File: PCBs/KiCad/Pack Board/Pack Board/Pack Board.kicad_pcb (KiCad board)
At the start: 2 copper layers, 10 parts, among them J4 BAR, J5 DISP, U1 Teensy4.0_AudioShield_REVD, U2 74AHC125

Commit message: Wand Board Updates
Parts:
- added J1: VENT LIGHTS, Connector_JST:JST_XH_B3B-XH-A_1x03_P2.50mm_Vertical, F.Cu at (251.2, 127.7)
- added J10: SND OUT, Connector_JST:JST_XH_B2B-XH-A_1x02_P2.50mm_Vertical, F.Cu at (181.9, 93.6)
- added J11: SND IN R, Connector_JST:JST_XH_B2B-XH-A_1x02_P2.50mm_Vertical, F.Cu at (205.7, 133.0)
- added J12: SND IN L, Connector_JST:JST_XH_B2B-XH-A_1x02_P2.50mm_Vertical, F.Cu at (205.7, 140.8)
- added J13: BT MOSFET, Connector_JST:JST_XH_B3B-XH-A_1x03_P2.50mm_Vertical, F.Cu at (251.2, 151.1)
- added J14: VENT MOSFET, Connector_JST:JST_XH_B3B-XH-A_1x03_P2.50mm_Vertical, F.Cu at (251.2, 158.9)
- added J15: ROT ENC, Connector_JST:JST_XH_B3B-XH-A_1x03_P2.50mm_Vertical, F.Cu at (251.2, 166.7)
- added J16: ROT SW, Connector_JST:JST_XH_B2B-XH-A_1x02_P2.50mm_Vertical, F.Cu at (205.7, 148.6)
- added J17: ION SW, Connector_JST:JST_XH_B2B-XH-A_1x02_P2.50mm_Vertical, F.Cu at (126.5, 145.5)
- added J2: PCELL LIGHTS, Connector_JST:JST_XH_B3B-XH-A_1x03_P2.50mm_Vertical, F.Cu at (155.5, 145.5)
- added J3: CYCLO LIGHTS, Connector_JST:JST_XH_B3B-XH-A_1x03_P2.50mm_Vertical, F.Cu at (251.2, 143.3)
- added J6: SERIAL, TerminalBlock_Phoenix:TerminalBlock_Phoenix_MKDS-1,5-2_1x02_P5.00mm_Horizontal, F.Cu at (137.5, 87.0)
- added J7: POW_IN, TerminalBlock_Phoenix:TerminalBlock_Phoenix_MKDS-1,5-2_1x02_P5.00mm_Horizontal, F.Cu at (106.0, 110.0)
- added J8: WAND PWR, TerminalBlock_Phoenix:TerminalBlock_Phoenix_MKDS-1,5-2_1x02_P5.00mm_Horizontal, F.Cu at (149.0, 87.0)
- added J9: AMP VOL, Connector_JST:JST_XH_B4B-XH-A_1x04_P2.50mm_Vertical, F.Cu at (227.2, 125.2)
- added REF**: MountingHole_3.2mm_M3_DIN965_Pad, MountingHole:MountingHole_3.2mm_M3_DIN965_Pad, F.Cu at (105.0, 145.0)
- added REF**: MountingHole_3.2mm_M3_DIN965_Pad, MountingHole:MountingHole_3.2mm_M3_DIN965_Pad, F.Cu at (170.0, 85.0)
- added REF**: MountingHole_3.2mm_M3_DIN965_Pad, MountingHole:MountingHole_3.2mm_M3_DIN965_Pad, F.Cu at (170.0, 145.0)
- added REF**: MountingHole_3.2mm_M3_DIN965_Pad, MountingHole:MountingHole_3.2mm_M3_DIN965_Pad, F.Cu at (105.0, 85.0)
- moved R4 147.0 mm to (243.1, 33.9), turned to -90 degrees
- moved R5 144.9 mm to (239.0, 33.9), turned to -90 degrees
- moved J4 123.1 mm to (237.1, 62.1)
- moved J5 123.1 mm to (237.1, 69.9)
- moved R3 103.3 mm to (199.6, 39.5), turned to 180 degrees
- moved C1 97.4 mm to (183.5, 37.0)
- moved R2 89.2 mm to (192.3, 56.0), turned to 180 degrees
- moved U2 62.2 mm to (166.5, 37.5)
- moved U1 51.6 mm to (131.0, 106.0), turned to -90 degrees
- moved R1 39.3 mm to (138.0, 52.5)
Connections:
- C1 pad 1: Net-(J1-Pin_2) -> +5V
- C1 pad 2: Net-(J1-Pin_1) -> GND
- J4 pad 1: Net-(J4-Pin_1) -> GND
- J4 pad 2: Net-(J4-Pin_2) -> +3.3V
- J4 pad 4: /SCL -> Net-(J4-Pin_4)
- J5 pad 1: Net-(J4-Pin_1) -> GND
- J5 pad 2: Net-(J4-Pin_2) -> +3.3V
- J5 pad 4: /SCL -> Net-(J4-Pin_4)
- R4 pad 2: Net-(J4-Pin_2) -> +3.3V
- R5 pad 1: /SCL -> Net-(J4-Pin_4)
- R5 pad 2: Net-(J4-Pin_2) -> +3.3V
- U1 pad 1: unconnected-(U1-GND-Pad1) -> GND
- U1 pad 11: unconnected-(U1-9_OUT1C-Pad11) -> Net-(J16-Pin_2)
- U1 pad 18: unconnected-(U1-14_A0_TX3_SPDIF_OUT-Pad18) -> Net-(U1-14_A0_TX3_SPDIF_OUT)
- U1 pad 2: unconnected-(U1-0_RX1_CRX2_CS1-Pad2) -> /RX
- U1 pad 20: unconnected-(U1-16_A2_RX4_SCL1-Pad20) -> Net-(U1-16_A2_RX4_SCL1)
- U1 pad 21: unconnected-(U1-17_A3_TX4_SDA1-Pad21) -> Net-(U1-17_A3_TX4_SDA1)
- U1 pad 22: unconnected-(U1-18_A4_SDA0-Pad22) -> /SDA
- U1 pad 23: unconnected-(U1-19_A5_SCL0-Pad23) -> Net-(J4-Pin_4)
- U1 pad 26: unconnected-(U1-22_A8_CTX1-Pad26) -> Net-(J17-Pin_2)
- U1 pad 28: unconnected-(U1-3V-Pad28) -> +3.3V
- U1 pad 29: unconnected-(U1-GND-Pad29) -> GND
- U1 pad 3: unconnected-(U1-1_TX1_CTX2_MISO1-Pad3) -> /TX
- U1 pad 30: unconnected-(U1-5V-Pad30) -> +5V
- U1 pad 31: unconnected-(U1-LINE_OUT_L-Pad31) -> Net-(J10-Pin_2)
- U1 pad 32: unconnected-(U1-LINE_OUT_GND-Pad32) -> Net-(J10-Pin_1)
- U1 pad 34: unconnected-(U1-LINE_IN_R-Pad34) -> Net-(J11-Pin_2)
- U1 pad 35: unconnected-(U1-LINE_IN_L-Pad35) -> Net-(J12-Pin_2)
- U1 pad 36: unconnected-(U1-LINE_IN_R_GND-Pad36) -> Net-(J11-Pin_1)
- U1 pad 37: unconnected-(U1-LINE_IN_L_GND-Pad37) -> Net-(J12-Pin_1)
- U1 pad 4: unconnected-(U1-2_OUT2-Pad4) -> Net-(J15-Pin_1)
- U1 pad 5: unconnected-(U1-3_LRCLK2-Pad5) -> Net-(J13-Pin_3)
- U1 pad 6: unconnected-(U1-4_BCLK2-Pad6) -> Net-(J15-Pin_3)
- U1 pad 7: unconnected-(U1-5_IN2-Pad7) -> Net-(J14-Pin_3)
- U2 pad 10: unconnected-(U2-3OE-Pad10) -> GND
- U2 pad 12: unconnected-(U2-4A-Pad12) -> Net-(U1-14_A0_TX3_SPDIF_OUT)
- U2 pad 13: Net-(U2-2OE) -> GND
- U2 pad 14: unconnected-(U2-VCC-Pad14) -> +5V
- U2 pad 4: Net-(U2-2OE) -> GND
- U2 pad 5: unconnected-(U2-2A-Pad5) -> Net-(U1-17_A3_TX4_SDA1)
- U2 pad 7: Net-(U2-2OE) -> GND
- U2 pad 9: unconnected-(U2-3A-Pad9) -> Net-(U1-16_A2_RX4_SCL1)
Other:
- board outline added: 75 x 70 mm

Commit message: Added motor output for wand rumble
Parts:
- added J18: i2c Extend, Connector_JST:JST_XH_B4B-XH-A_1x04_P2.50mm_Vertical, F.Cu at (227.2, 117.0)

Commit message: Added additional i2c output to wand board for optional driver
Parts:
- removed J4: BAR, Connector_JST:JST_XH_B4B-XH-A_1x04_P2.50mm_Vertical
- removed J5: DISP, Connector_JST:JST_XH_B4B-XH-A_1x04_P2.50mm_Vertical
- moved J18 30.1 mm to (237.5, 88.8)
- moved J9 25.8 mm to (237.5, 101.5)
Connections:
- net Net-(J18-Pin_4) renamed /SCL
- U1 pad 45: (no net) -> unconnected-(U1-NCB-Pad45)
- U1 pad 46: (no net) -> unconnected-(U1-NCA-Pad46)

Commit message: Pack Board 2.0
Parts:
- moved J15 160.3 mm to (104.2, 102.8)
- moved J13 152.0 mm to (104.2, 112.5)
- moved J3 139.9 mm to (120.2, 94.2)
- moved J1 137.9 mm to (120.2, 84.5)
- moved C1 125.6 mm to (106.0, 135.8)
- moved J14 120.5 mm to (156.5, 84.5)
- moved R3 120.1 mm to (118.2, 127.9), turned to 90 degrees
- moved J16 114.5 mm to (105.5, 93.2)
- moved R4 111.9 mm to (151.1, 97.8), turned to 180 degrees
- moved R5 111.0 mm to (151.1, 101.8), turned to 180 degrees
- moved R2 100.9 mm to (121.5, 127.9), turned to 90 degrees
- moved U2 82.3 mm to (114.8, 101.5)
- moved J9 80.4 mm to (157.5, 93.5), turned to -90 degrees
- moved R1 78.8 mm to (115.0, 127.9), turned to 90 degrees
- moved J18 70.7 mm to (167.0, 93.5), turned to -90 degrees
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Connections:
- net /SCL renamed Net-(J18-Pin_4)
- net Net-(J10-Pin_1) renamed /LINE_OUT_GND
- net Net-(J11-Pin_1) renamed /LINE_IN_R_GND
- net Net-(J11-Pin_2) renamed /LINE_IN_R
- net Net-(J12-Pin_1) renamed /LINE_IN_L_GND
- net Net-(J12-Pin_2) renamed /LINE_IN_L
- J10 pad 2: Net-(J10-Pin_2) -> /LINE_OUT_L
- U1 pad 11: Net-(J16-Pin_2) -> Net-(J13-Pin_3)
- U1 pad 31: Net-(J10-Pin_2) -> /LINE_OUT_L
- U1 pad 4: Net-(J15-Pin_1) -> Net-(J16-Pin_2)
- U1 pad 46: unconnected-(U1-NCA-Pad46) -> /LINE_OUT_L
- U1 pad 5: Net-(J13-Pin_3) -> Net-(J15-Pin_3)
- U1 pad 6: Net-(J15-Pin_3) -> Net-(J15-Pin_1)
- U2 pad 12: Net-(U1-14_A0_TX3_SPDIF_OUT) -> Net-(U1-17_A3_TX4_SDA1)
- U2 pad 5: Net-(U1-17_A3_TX4_SDA1) -> Net-(U1-14_A0_TX3_SPDIF_OUT)
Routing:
- net +3.3V: track 0.00 -> 167.0 mm
- net +5V: track 0.00 -> 156.9 mm
- net Net-(J16-Pin_2): track 0.00 -> 63.1 mm
- net Net-(J17-Pin_2): track 0.00 -> 63.1 mm
- net Net-(U1-14_A0_TX3_SPDIF_OUT): track 0.00 -> 61.9 mm
- net Net-(J15-Pin_1): track 0.00 -> 55.6 mm
- net Net-(J15-Pin_3): track 0.00 -> 53.4 mm
- net Net-(J14-Pin_3): track 0.00 -> 51.2 mm
- net Net-(J1-Pin_3): track 0.00 -> 48.4 mm
- net /SDA: track 0.00 -> 47.3 mm
- net Net-(J13-Pin_3): track 0.00 -> 43.6 mm
- net Net-(U1-17_A3_TX4_SDA1): track 0.00 -> 40.8 mm
- net Net-(J18-Pin_4): track 0.00 -> 39.2 mm
- net Net-(U1-16_A2_RX4_SCL1): track 0.00 -> 38.7 mm
- net Net-(J3-Pin_3): track 0.00 -> 37.1 mm
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- added copper zone on B.Cu, net GND
- added copper zone on F.Cu, net GND
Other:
- board text added: "3.3"
- board text added: "3.3V"
- board text added: "5V"
- board text added: "A"
- board text added: "AG"
- board text added: "B"
- board text added: "D"
- board text added: "G"
- board text added: "JLCJLCJLCJLC"
- board text added: "RX"
- board text added: "SCL"
- board text added: "SDA"
- board text added: "Sig"
- board text added: "TX"
- board text added: "Teensy Pack Board 2.0"

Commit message: Updated PCBs for ESP32 Wand Build
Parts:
- moved J2 5.46 mm to (161.0, 145.5)
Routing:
- net Net-(J2-Pin_3): track 36.3 -> 41.8 mm

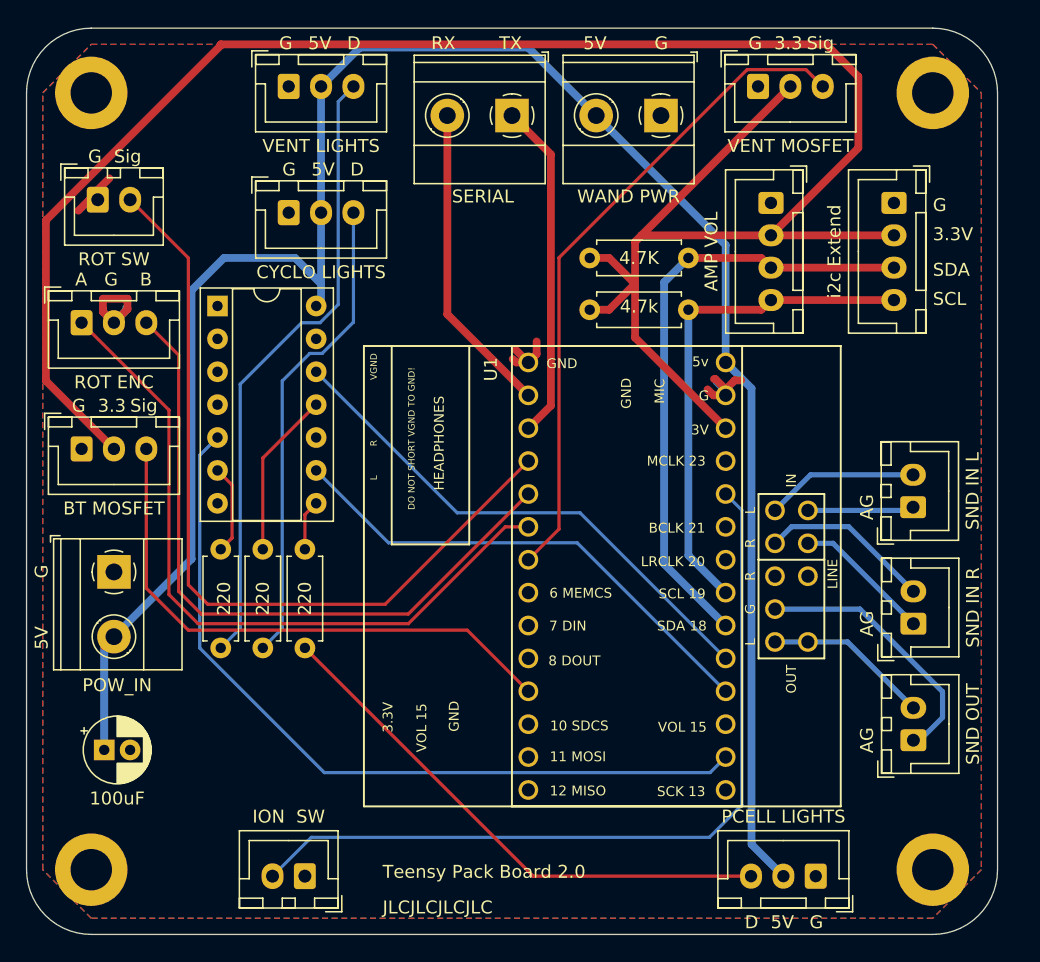
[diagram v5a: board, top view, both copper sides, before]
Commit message: Pack PCB tweaks for 5V triggered FET/Relays, consolidating LED pins, and breaking out newly freed  I/O pin.  Re-jigged board layout and fixed some dimensions.
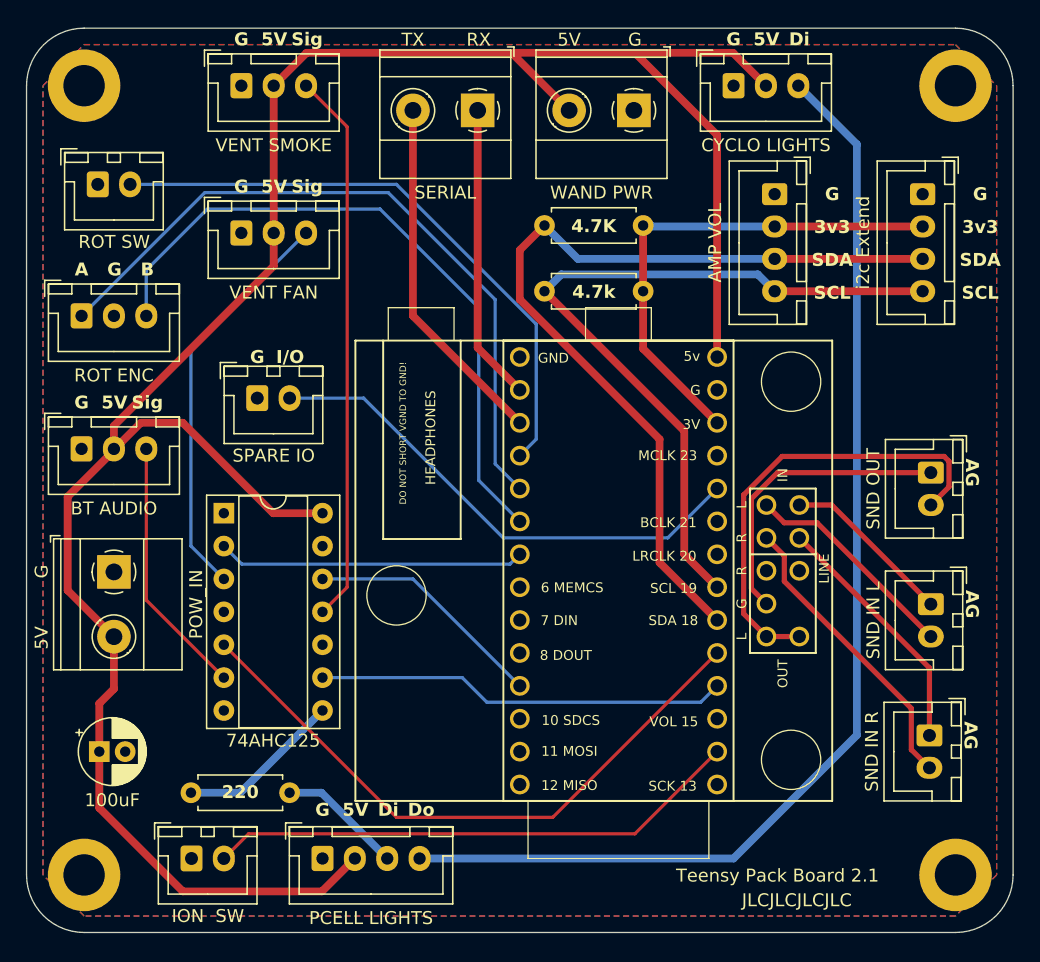
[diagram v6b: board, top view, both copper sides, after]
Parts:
- removed J2: PCELL LIGHTS, Connector_JST:JST_XH_B3B-XH-A_1x03_P2.50mm_Vertical
- removed R1, R3: 220, Resistor_THT:R_Axial_DIN0207_L6.3mm_D2.5mm_P7.62mm_Horizontal
- added J4: PCELL LIGHTS, ProtonPackFootprints:JST_XH_B4B-XH-A_1x04_NeoPixelHeader, F.Cu at (122.9, 144.1)
- added J5: SPARE IO, ProtonPackFootprints:JST_XH_B2B-XH-A_1x02_P2.50mm_Vertical, F.Cu at (117.8, 108.6)
- J1: value VENT LIGHTS -> VENT SMOKE; footprint Connector_JST:JST_XH_B3B-XH-A_1x03_P2.50mm_Vertical -> ProtonPackFootprints:JST_XH_B3B-XH-A_1x03_MosRelay
- J10, J11, J12: footprint Connector_JST:JST_XH_B2B-XH-A_1x02_P2.50mm_Vertical -> ProtonPackFootprints:JST_XH_B2B-XH-A_1x02_AudioHeader
- J13: value BT MOSFET -> BT AUDIO; footprint Connector_JST:JST_XH_B3B-XH-A_1x03_P2.50mm_Vertical -> ProtonPackFootprints:JST_XH_B3B-XH-A_1x03_MosRelay
- J14: value VENT MOSFET -> VENT FAN; footprint Connector_JST:JST_XH_B3B-XH-A_1x03_P2.50mm_Vertical -> ProtonPackFootprints:JST_XH_B3B-XH-A_1x03_MosRelay
- J15: footprint Connector_JST:JST_XH_B3B-XH-A_1x03_P2.50mm_Vertical -> ProtonPackFootprints:JST_XH_B3B-XH-A_1x03_RotEncoder
- J16, J17: footprint Connector_JST:JST_XH_B2B-XH-A_1x02_P2.50mm_Vertical -> ProtonPackFootprints:JST_XH_B2B-XH-A_1x02_P2.50mm_Vertical
- J18, J9: footprint Connector_JST:JST_XH_B4B-XH-A_1x04_P2.50mm_Vertical -> ProtonPackFootprints:JST_XH_B4B-XH-A_1x04_i2cHeader
- J3: footprint Connector_JST:JST_XH_B3B-XH-A_1x03_P2.50mm_Vertical -> ProtonPackFootprints:JST_XH_B3B-XH-A_1x03_NeoPixelHeader
- J6, J7, J8: footprint TerminalBlock_Phoenix:TerminalBlock_Phoenix_MKDS-1,5-2_1x02_P5.00mm_Horizontal -> ProtonPackFootprints:TerminalBlock_Phoenix_MKDS-1,5-2_1x02_P5.00mm_Horizontal
- R2, R4, R5: footprint Resistor_THT:R_Axial_DIN0207_L6.3mm_D2.5mm_P7.62mm_Horizontal -> ProtonPackFootprints:R_Axial_DIN0207_L6.3mm_D2.5mm_P7.62mm_Horizontal
- REF** (x4): footprint MountingHole:MountingHole_3.2mm_M3_DIN965_Pad -> ProtonPackFootprints:MountingHole_3.2mm_M3_DIN965_Pad
- U1: footprint Teensy:4.0audioshield -> ProtonPackFootprints:Teensy Audioshield Rev D
- moved J14 41.5 mm to (116.6, 95.8)
- moved J3 35.7 mm to (154.6, 84.4)
- moved J10 20.7 mm to (169.8, 114.3), turned to -90 degrees
- moved U2 16.0 mm to (115.2, 117.5)
- moved R4 11.4 mm to (140.0, 95.2), turned to 0 degrees
- moved R2 11.2 mm to (120.3, 139.1), turned to 180 degrees
- moved R5 11.2 mm to (140.0, 100.3), turned to 0 degrees
- moved J17 8.87 mm to (112.7, 144.1), turned to 0 degrees
- moved J11 8.72 mm to (169.7, 134.6), turned to -90 degrees
- moved J12 7.62 mm to (169.8, 124.5), turned to -90 degrees
- moved J1 3.66 mm to (116.6, 84.4)
- moved J6 2.68 mm to (134.8, 86.3)
- moved J18 2.32 mm to (169.2, 92.8)
- moved J8 2.13 mm to (146.9, 86.3)
- moved REF** 1.84 mm to (171.8, 84.4)
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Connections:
- net Net-(J18-Pin_4) renamed /SCL
- net Net-(U2-3Y) renamed /LED_IN
- J13 pad 2: +3.3V -> +5V
- J14 pad 2: +3.3V -> +5V
- J3 pad 3: Net-(J3-Pin_3) -> /CYCLO_LED_IN
- R2 pad 1: Net-(J2-Pin_3) -> /PCELL_LED_IN
- U1 pad 11: Net-(J13-Pin_3) -> Net-(U1-9_OUT1C)
- U1 pad 18: Net-(U1-14_A0_TX3_SPDIF_OUT) -> Net-(J17-Pin_2)
- U1 pad 2: /RX -> /TX
- U1 pad 26: Net-(J17-Pin_2) -> Net-(J5-Pin_2)
- U1 pad 3: /TX -> /RX
- U1 pad 5: Net-(J15-Pin_3) -> Net-(J15-Pin_1)
- U1 pad 6: Net-(J15-Pin_1) -> Net-(J15-Pin_3)
- U1 pad 7: Net-(J14-Pin_3) -> Net-(U1-5_IN2)
- U2 pad 1: unconnected-(U2-1OE-Pad1) -> GND
- U2 pad 11: Net-(U2-4Y) -> Net-(J1-Pin_3)
- U2 pad 12: Net-(U1-17_A3_TX4_SDA1) -> Net-(U1-9_OUT1C)
- U2 pad 2: unconnected-(U2-1A-Pad2) -> Net-(U1-5_IN2)
- U2 pad 3: unconnected-(U2-1Y-Pad3) -> Net-(J14-Pin_3)
- U2 pad 5: Net-(U1-14_A0_TX3_SPDIF_OUT) -> Net-(U1-17_A3_TX4_SDA1)
- U2 pad 6: Net-(U2-2Y) -> Net-(J13-Pin_3)
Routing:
- net +3.3V: track 167.0 -> 39.4 mm
- net /CYCLO_LED_IN: track 0.00 -> 89.8 mm
- net Net-(U1-14_A0_TX3_SPDIF_OUT): track 61.9 -> 0.00 mm
- net Net-(J2-Pin_3): track 41.8 -> 0.00 mm
- net Net-(J5-Pin_2): track 0.00 -> 39.1 mm
- net Net-(J3-Pin_3): track 37.1 -> 0.00 mm
- net GND: track 24.0 -> 0.00 mm
- net Net-(U1-5_IN2): track 0.00 -> 23.8 mm
- net +5V: track 156.7 -> 180.2 mm
- net Net-(J13-Pin_3): track 43.6 -> 20.1 mm
- net /LINE_OUT_L: track 12.8 -> 35.4 mm
- net Net-(J17-Pin_2): track 63.1 -> 41.5 mm
- net /SDA: track 47.3 -> 67.9 mm
- net Net-(J14-Pin_3): track 51.2 -> 31.5 mm
- net /SCL: track 39.2 -> 58.7 mm
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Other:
- board size 75 x 70 mm -> 76.2 x 69.8 mm
- board text added: "LRCLK 20"
- board text added: "Teensy Pack Board 2.1"
- board text removed: "3.3"
- board text removed: "3.3V"
- board text removed: "A"
- board text removed: "AG"
- board text removed: "B"
- board text removed: "D"
- board text removed: "SCL"
- board text removed: "SDA"
- board text removed: "Sig"
- board text removed: "Teensy Pack Board 2.0"
